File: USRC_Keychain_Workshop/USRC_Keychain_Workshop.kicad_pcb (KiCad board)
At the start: 4 copper layers, 120.1 x 96.7 mm, 29 parts, among them U1 ICM7555xB, U2 4017

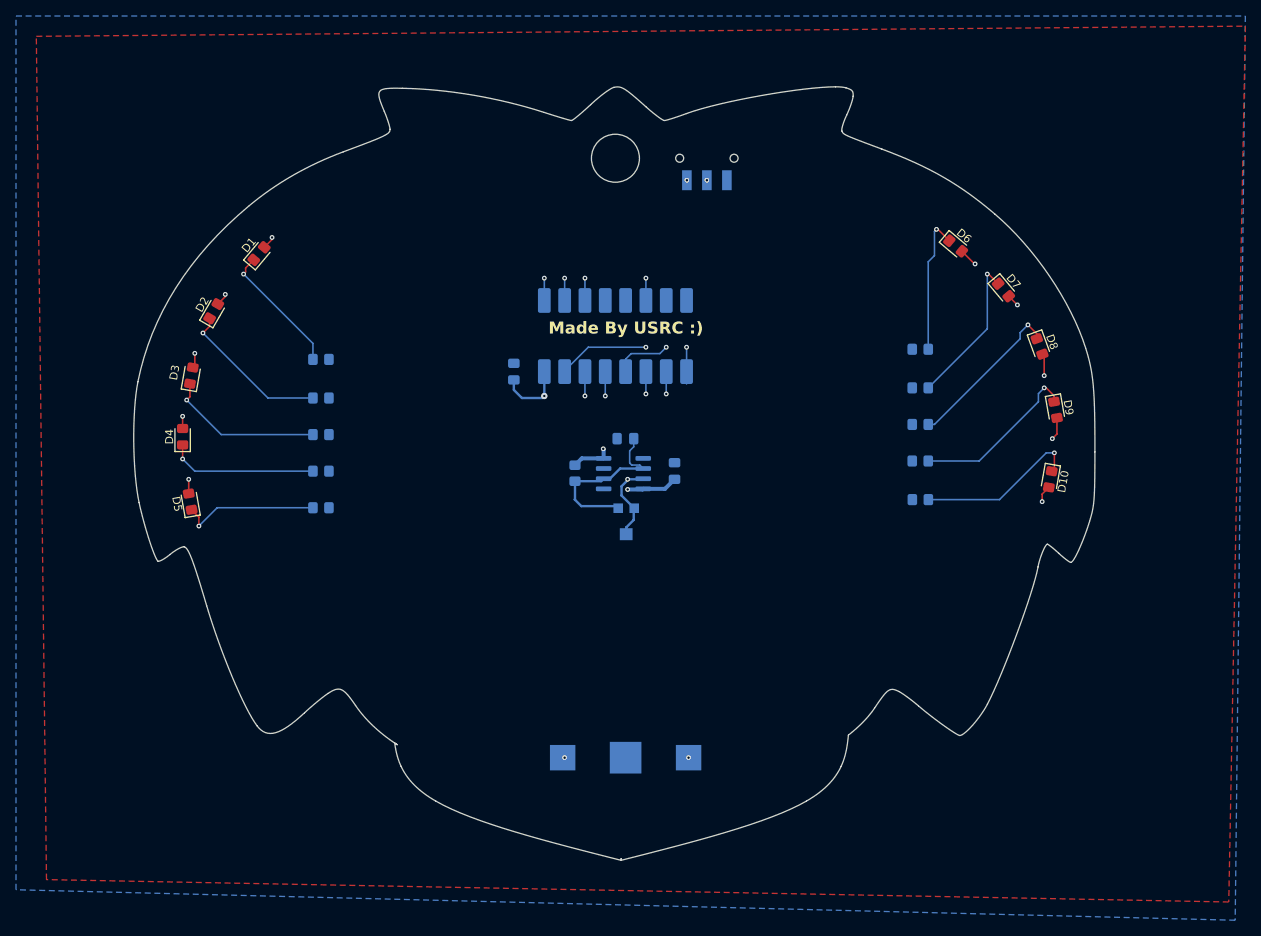
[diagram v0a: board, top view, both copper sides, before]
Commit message: USRC_Keychain_Workshop version 2
Uploaded Version 2, a more trimmed down version of the KiCAD Keychain PCB Workshop, open the project from the KiCAD Project File.
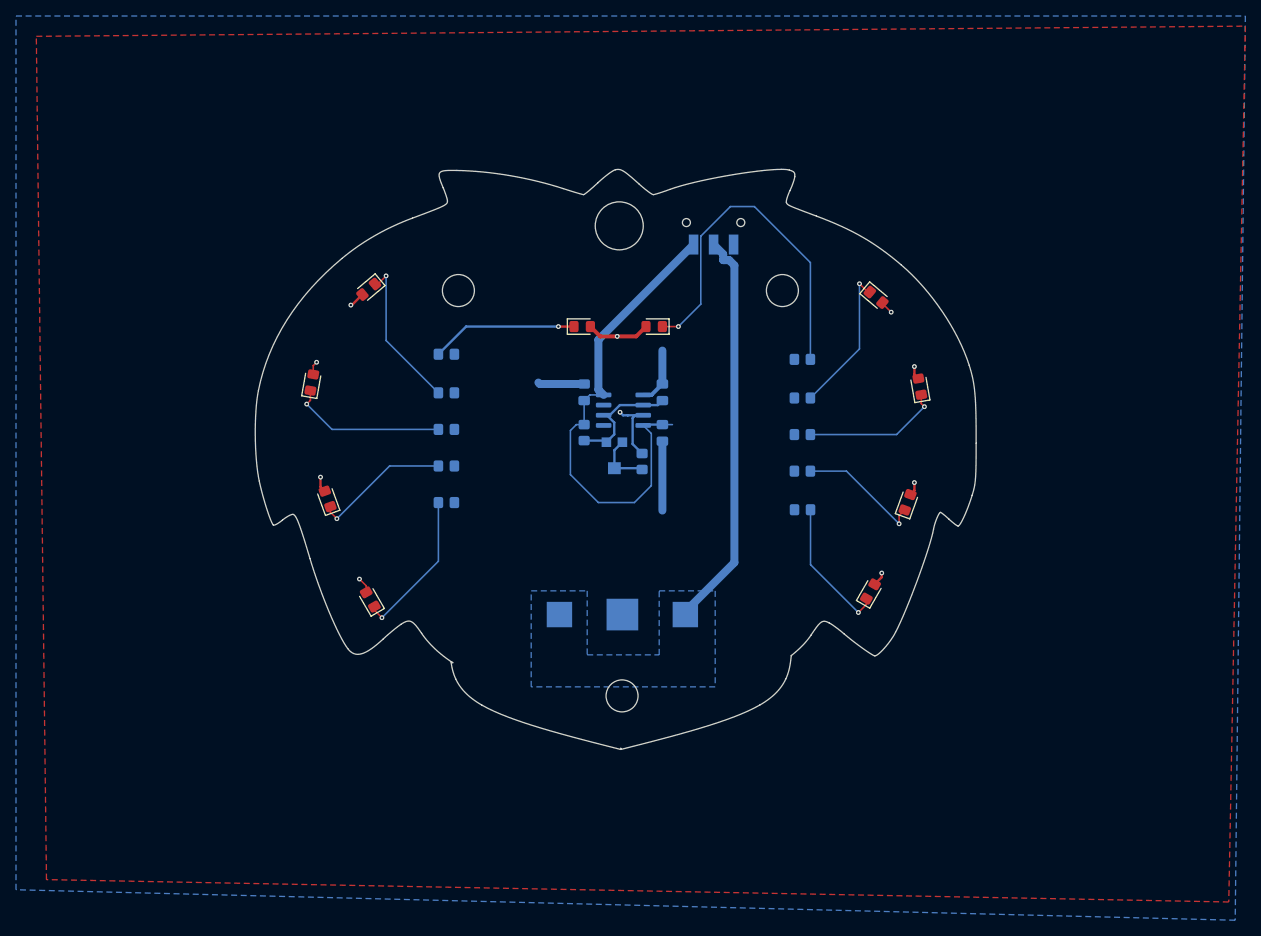
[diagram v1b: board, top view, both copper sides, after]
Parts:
- removed U2: 4017, Package_DIP:DIP-16_W8.89mm_SMDSocket_LongPads
- added R1: 1k, Resistor_SMD:R_0805_2012Metric_Pad1.20x1.40mm_HandSolder, B.Cu at (154.5, 98.9)
- C2: value 300n -> 2.2u
- RV1: value R_Potentiometer -> 1M
- moved D1 41.4 mm to (147.0, 82.0), turned to 0 degrees
- moved D6 39.0 mm to (156.0, 82.0), turned to 180 degrees
- moved D10 26.5 mm to (183.0, 115.1), turned to 60 degrees
- moved D5 25.6 mm to (120.5, 116.1), turned to 120 degrees
- moved D9 21.8 mm to (187.6, 104.0), turned to 70 degrees
- moved D4 19.7 mm to (115.1, 103.5), turned to 110 degrees
- moved D2 19.6 mm to (120.3, 77.3), turned to -140 degrees
- moved BT1 17.9 mm to (152.0, 118.0)
- moved D7 15.9 mm to (183.7, 78.3), turned to -40 degrees
- moved D8 15.8 mm to (189.2, 89.5), turned to 100 degrees
- moved R2 15.7 mm to (130.0, 85.5)
- moved R3 15.7 mm to (130.0, 90.3)
- moved R4 15.7 mm to (130.0, 94.9)
- moved R5 15.7 mm to (130.0, 99.4)
- moved R6 15.7 mm to (130.0, 104.0)
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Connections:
- D1 pad 2: Net-(D1-A) -> /555_OUT
- D10 pad 2: Net-(D10-A) -> /555_OUT
- D2 pad 2: Net-(D2-A) -> /555_OUT
- D3 pad 2: Net-(D3-A) -> /555_OUT
- D4 pad 2: Net-(D4-A) -> /555_OUT
- D5 pad 2: Net-(D5-A) -> /555_OUT
- D6 pad 2: Net-(D6-A) -> /555_OUT
- D7 pad 2: Net-(D7-A) -> /555_OUT
- D8 pad 2: Net-(D8-A) -> /555_OUT
- D9 pad 2: Net-(D9-A) -> /555_OUT
- RV1 pad 2: /555_OUT -> Net-(R1-Pad1)
- RV1 pad 3: /555_OUT -> Net-(R1-Pad1)
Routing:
- net /555_OUT: track 41.3 -> 197.5 mm, vias 2 -> 10
- net Net-(D5-A): track 80.5 -> 0.00 mm, vias 2 -> 0
- net Net-(D7-A): track 61.8 -> 0.00 mm, vias 2 -> 0
- net Net-(D10-A): track 60.0 -> 0.00 mm, vias 2 -> 0
- net Net-(D8-A): track 58.7 -> 0.00 mm, vias 2 -> 0
- net Net-(D4-A): track 58.2 -> 0.00 mm, vias 2 -> 0
- net Net-(D6-A): track 57.7 -> 0.00 mm, vias 2 -> 0
- net Net-(D9-A): track 56.2 -> 0.00 mm, vias 2 -> 0
- net Net-(D3-A): track 56.1 -> 0.00 mm, vias 2 -> 0
- net Net-(BT1-PadP1): track 99.2 -> 50.3 mm, vias 3 -> 0
- net Net-(D2-A): track 47.8 -> 0.00 mm, vias 2 -> 0
- net Net-(D1-A): track 44.7 -> 0.00 mm, vias 2 -> 0
- net Net-(D6-K): track 17.6 -> 44.7 mm
- net GND: track 0.00 -> 21.6 mm
- net +3.3V: track 79.0 -> 62.5 mm, vias 4 -> 0
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- added copper zone on B.Cu, net Net-(BT1-PadP1)
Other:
- board size 120.1 x 96.7 mm -> 90.1 x 72.5 mm
- board text added: "Designed By: P. M."
- board text added: "Made By USRC"
- board text removed: "Designed By: Parvez M."
- board text removed: "Made By USRC :)"

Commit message: Updated PCB Layout
Removed duplicate resistor and capacitor.
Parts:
- removed C3: 100n, Capacitor_SMD:C_0805_2012Metric_Pad1.18x1.45mm_HandSolder
- removed the R1 at (147.2, 95.3)
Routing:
- net GND: track 21.6 -> 12.9 mm
- net +3.3V: track 62.5 -> 55.8 mm
- net Net-(U1-THRES): track 15.5 -> 13.0 mm
